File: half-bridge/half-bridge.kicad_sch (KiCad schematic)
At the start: 102 parts, among them J1 Conn_01x11_Pin, J2 MountingHole_Pad, J3 Conn_01x11_Pin, J4 Conn_01x11_Pin, J5 Conn_01x11_Pin, J6 Conn_01x11_Pin, J7 MountingHole_Pad, J8 MountingHole_Pad, J9 MountingHole_Pad, Q1 EPC2306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

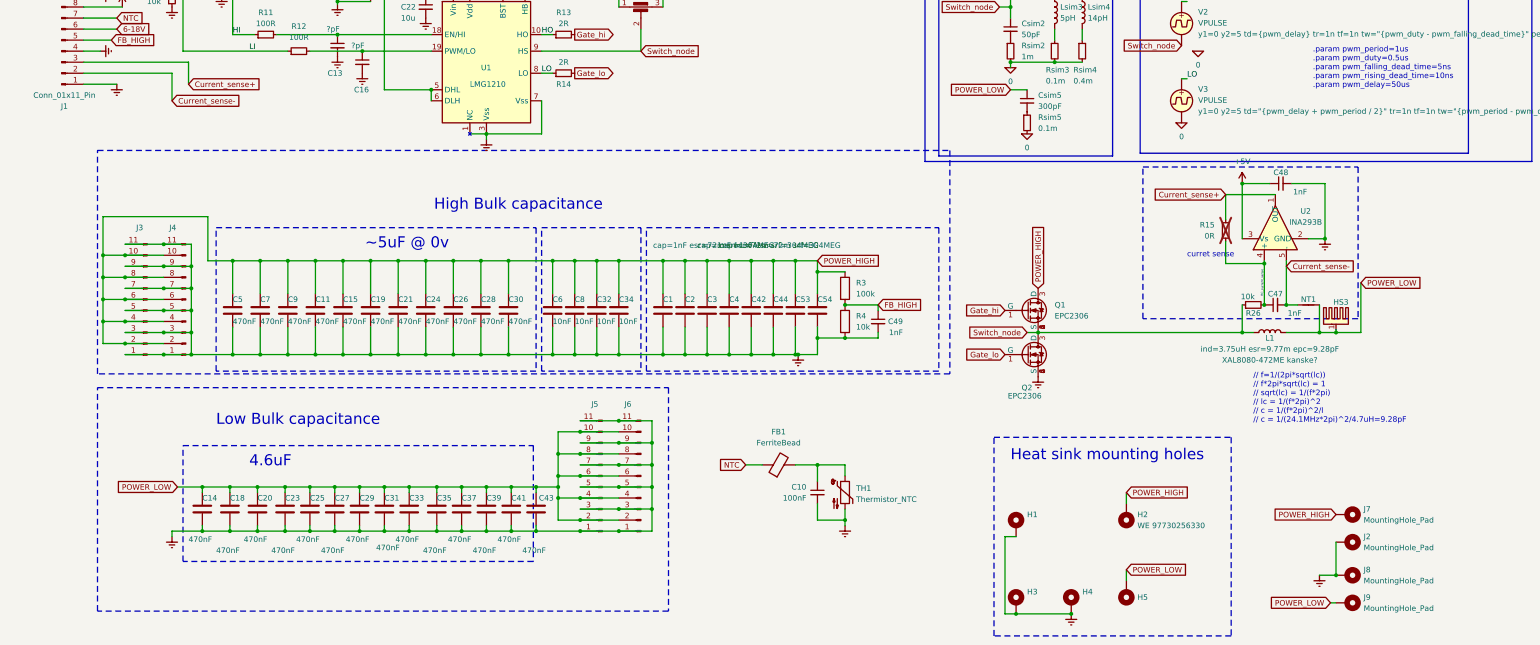
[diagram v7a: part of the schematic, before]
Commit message: Add diodes and make room for larger inductors
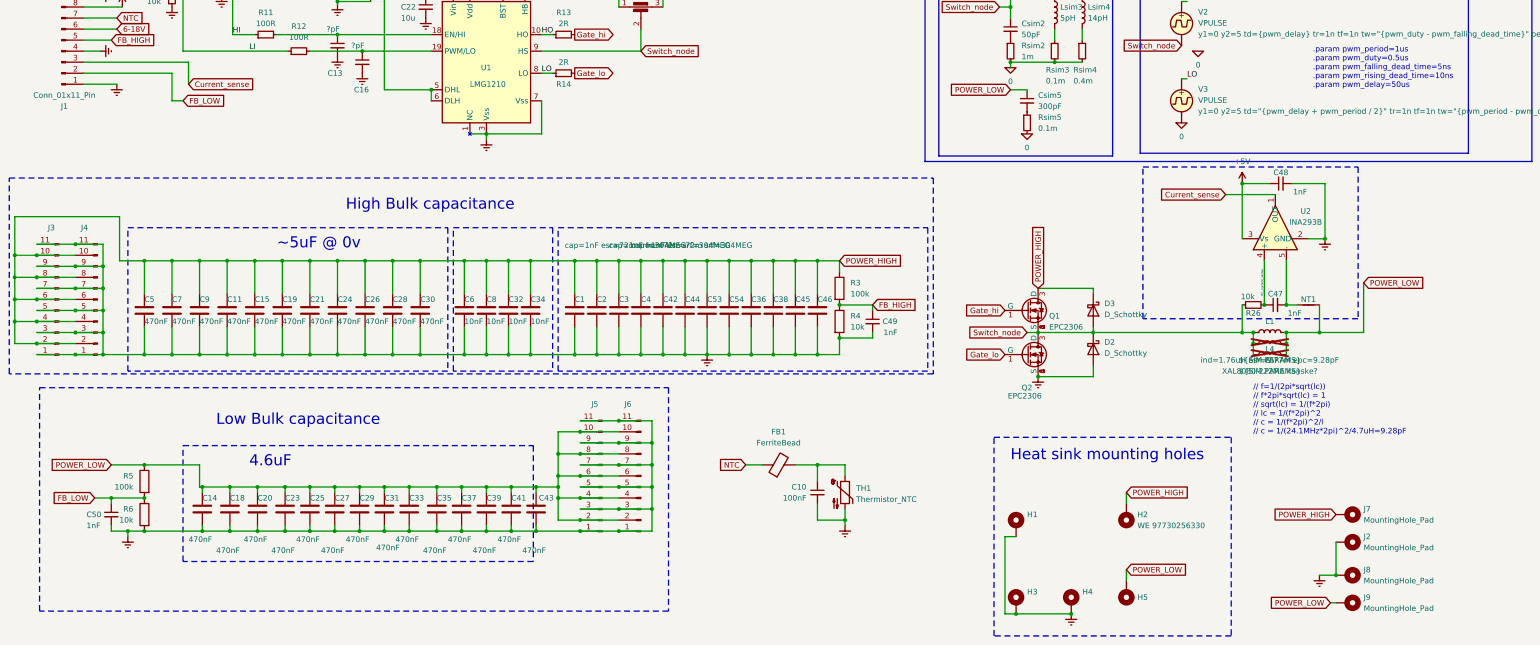
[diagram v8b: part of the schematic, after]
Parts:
- removed HS3: Heatsink_Pad, Library:Heatsink_SMD_Chamfered_5.2x5.2mm, symbol Mechanical:Heatsink_Pad
- removed R15: 0R, Library:SolderJumper-2_P1.3mm_Open_TrianglePad1.0x1.2mm, symbol Device:R_Small
- added C36, C38, C45, C46: ${SIM.PARAMS}, Capacitor_SMD:C_0402_1005Metric, symbol Device:C
- added C50: 1nF, Capacitor_SMD:C_0603_1608Metric, symbol Device:C_Small
- added D2, D3: D_Schottky, Diode_SMD:D_SMP_DO-220AA, symbol Device:D_Schottky
- added L4: ${SIM.PARAMS}, Inductor_SMD:L_Wuerth_WE-PD-Typ-LS, symbol Device:L
- added L5: ${SIM.PARAMS}, Inductor_SMD:L_Bourns_SRP1050WA, symbol Device:L
- added R5: 100k, Resistor_SMD:R_1206_3216Metric, symbol Device:R
- added R6: 10k, Resistor_SMD:R_0805_2012Metric, symbol Device:R
- L1: Field4 XAL8080-472ME kanske? -> XAL8080-222ME kanske?
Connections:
- net 0: now also C36.2, C38.2, C45.2, C46.2, C50.2, D2.2 (A), R6.2
- net POWER_HIGH: now also C36.1, C38.1, C45.1, C46.1, D3.1 (K)
- net POWER_LOW: now also L4.2, L5.2, R5.1
- net Switch_node: now also D2.1 (K), D3.2 (A), L4.1, L5.1
- net Current_sense+ renamed Current_sense
- net Current_sense-: no longer names the net of C47.2, NT1.1, U2.5 (-)
- net Current_sense-: no longer J1.2 (Pin_2)
- new net FB_LOW: C50.1, J1.2 (Pin_2), R5.2, R6.1
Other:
- note removed: "curret sense"
- moved on the sheet: C1, C11, C15, C19, C2, C21, C24, C26, C28, C3, C30, C32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
